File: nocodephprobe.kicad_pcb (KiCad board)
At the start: 2 copper layers, 76 x 80.9 mm, 30 parts, among them J1 RF1-01 BNC, J2 10K, Q1 2N7002, U1 LMV358a, U2 ICL7106CPL, U3 MCP1501-10xCH, U4 VI-302-DP-RC-S

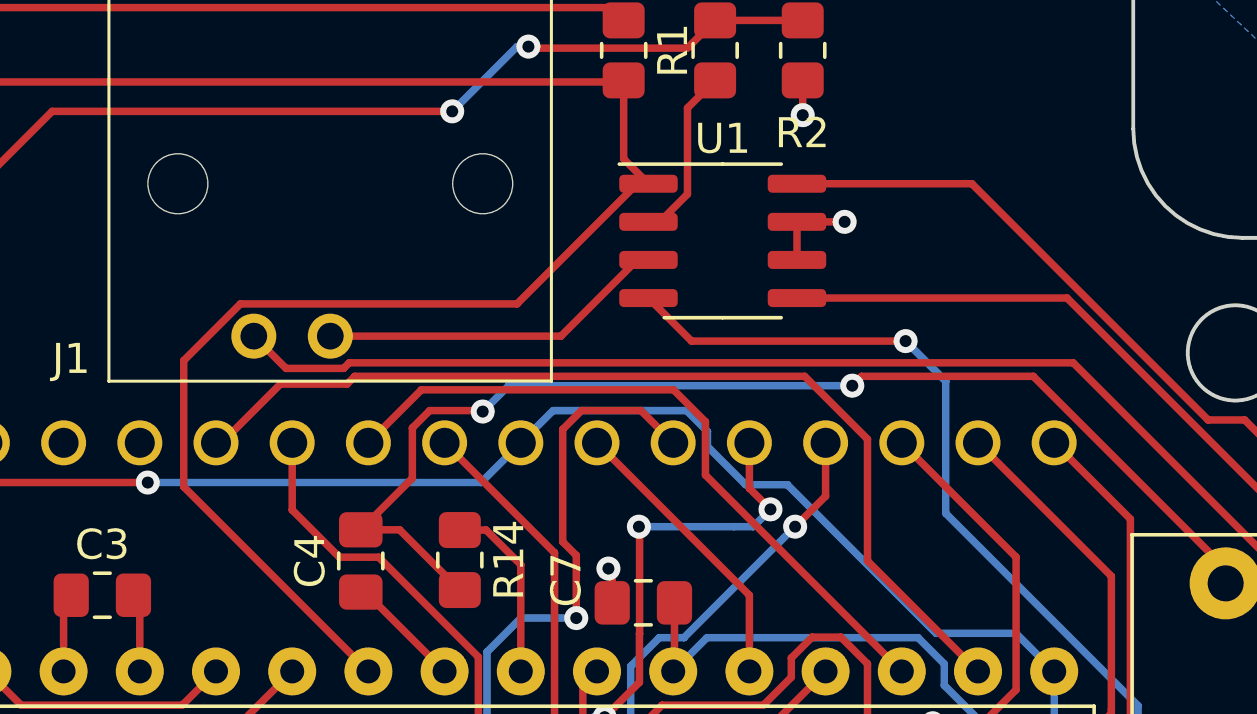
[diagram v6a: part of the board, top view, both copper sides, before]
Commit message: Add guard ring around probe input
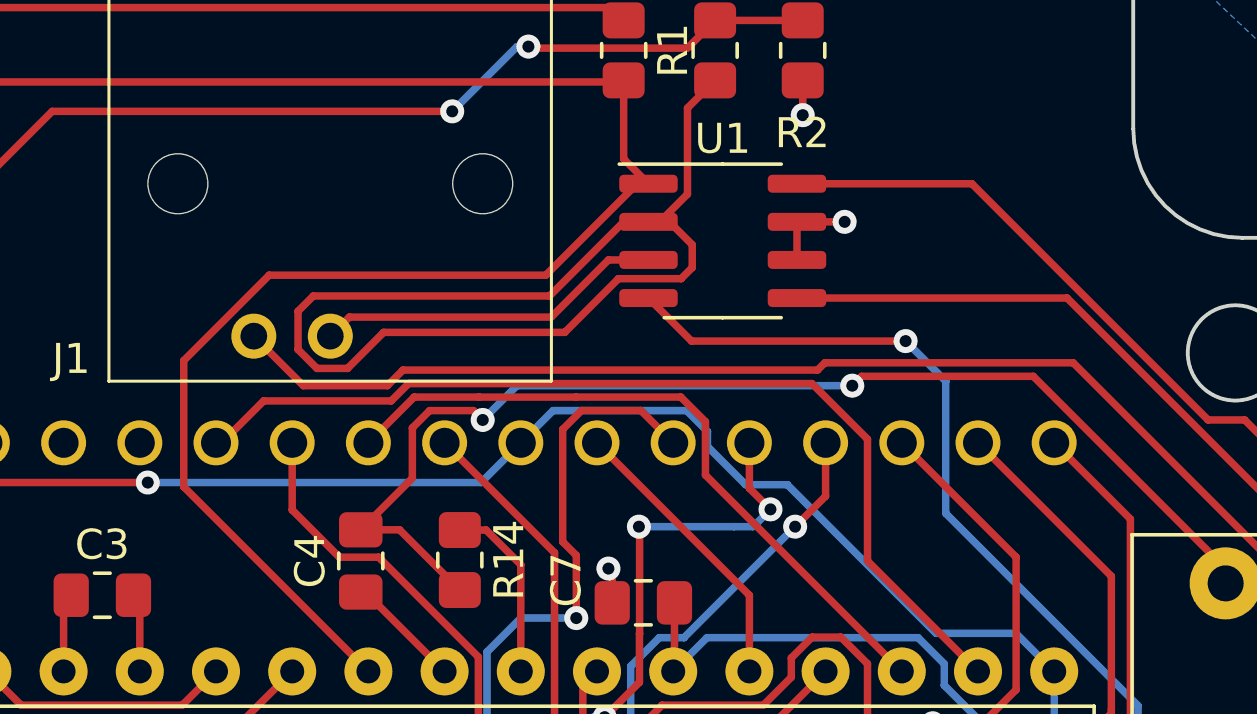
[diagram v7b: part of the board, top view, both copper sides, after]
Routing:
- net Net-(U1A--): track 5.86 -> 37.4 mm

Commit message: Correct Cref (C3 value)
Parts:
- C3: value .01uF -> 0.1uF
- U3: value MCP1501-10xCH -> MCP1501T-10E/CHY
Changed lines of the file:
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@@
         (effects (font (size 1 1) (thickness 0.15)))
     )
-    (fp_text value "MCP1501-10xCH" (at 0 2.4) (layer "F.Fab")
+    (fp_text value "MCP1501T-10E/CHY" (at 0 2.4) (layer "F.Fab")
         (effects (font (size 1 1) (thickness 0.15)))
     )
@@
         (effects (font (size 1 1) (thickness 0.15)))
     )
-    (fp_text value ".01uF" (at 0 1.68) (layer "F.Fab")
-        (effects (font (size 1 1) (thickness 0.15)))
-    )
+    (fp_text value "0.1uF" (at 0 1.68) (layer "F.Fab")
+        (effects (font (size 1 1) (thickness 0.15)))
+    )
